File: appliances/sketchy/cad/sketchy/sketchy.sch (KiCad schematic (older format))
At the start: 6 parts, among them J1 Barrel_Jack, M1 Stepper_Motor_bipolar, M2 Stepper_Motor_bipolar, U1 ESP32PICO-KIT

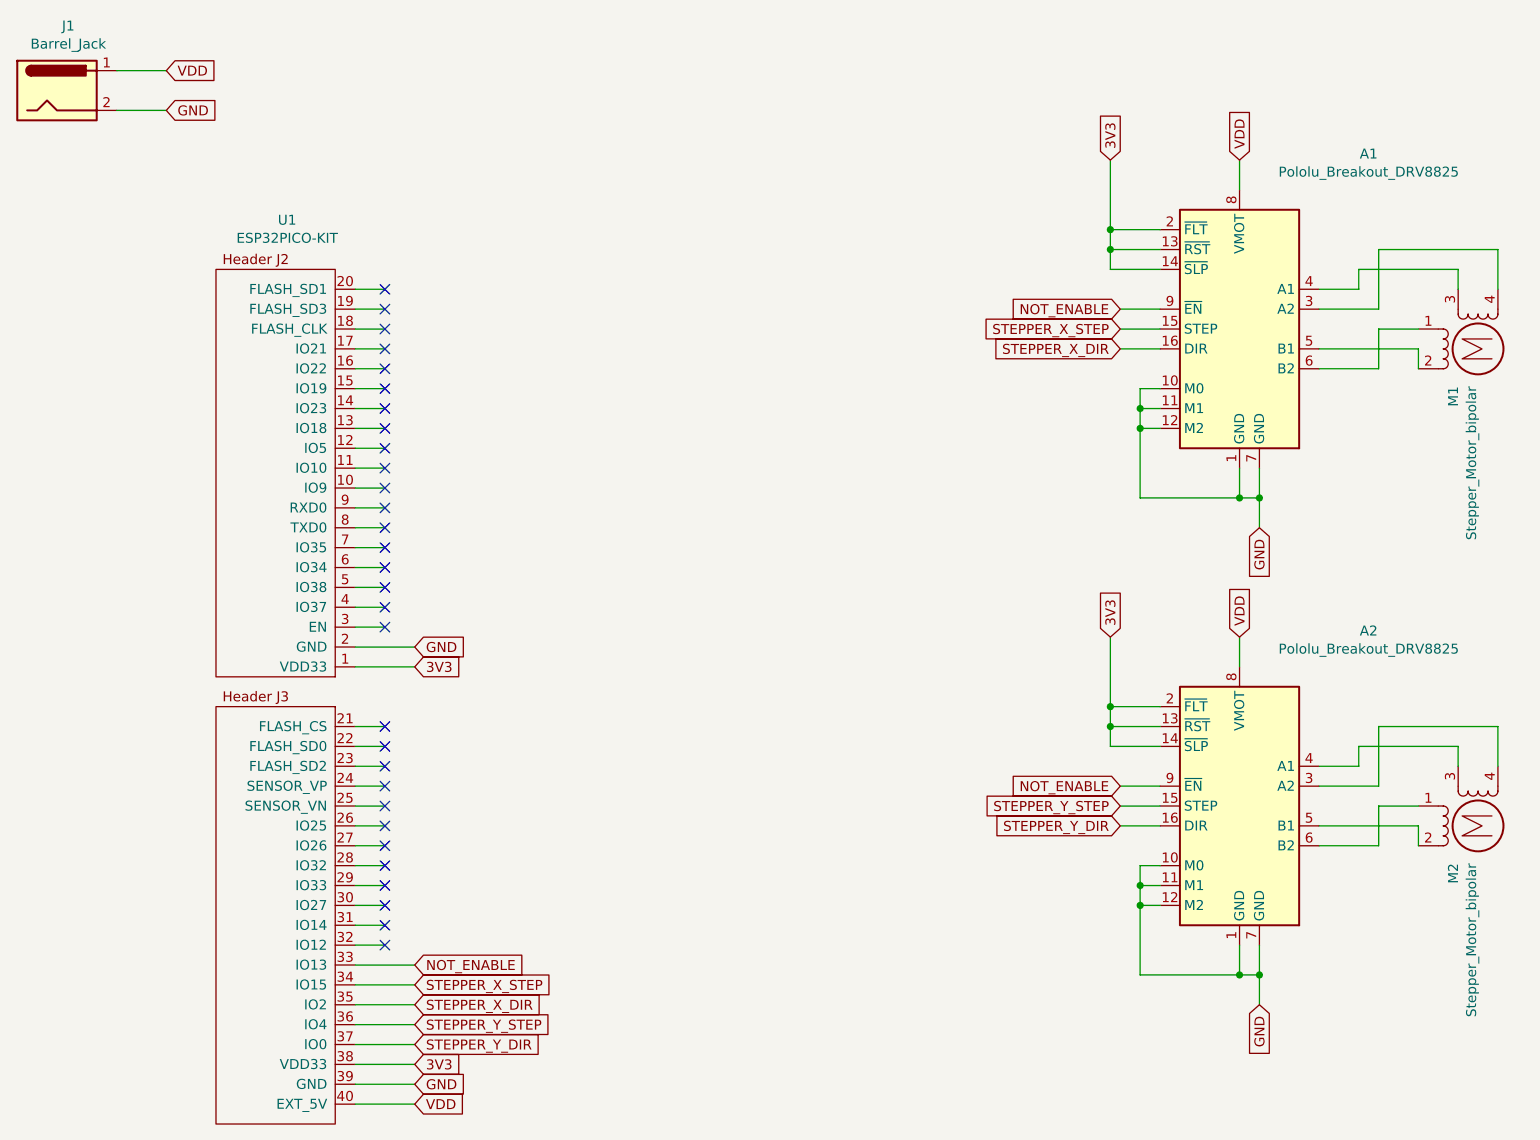
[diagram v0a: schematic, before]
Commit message: Changed stepper driver to the 4988 that I'm actually using, routed all tracks, and added silkscreen text and mounting holes.
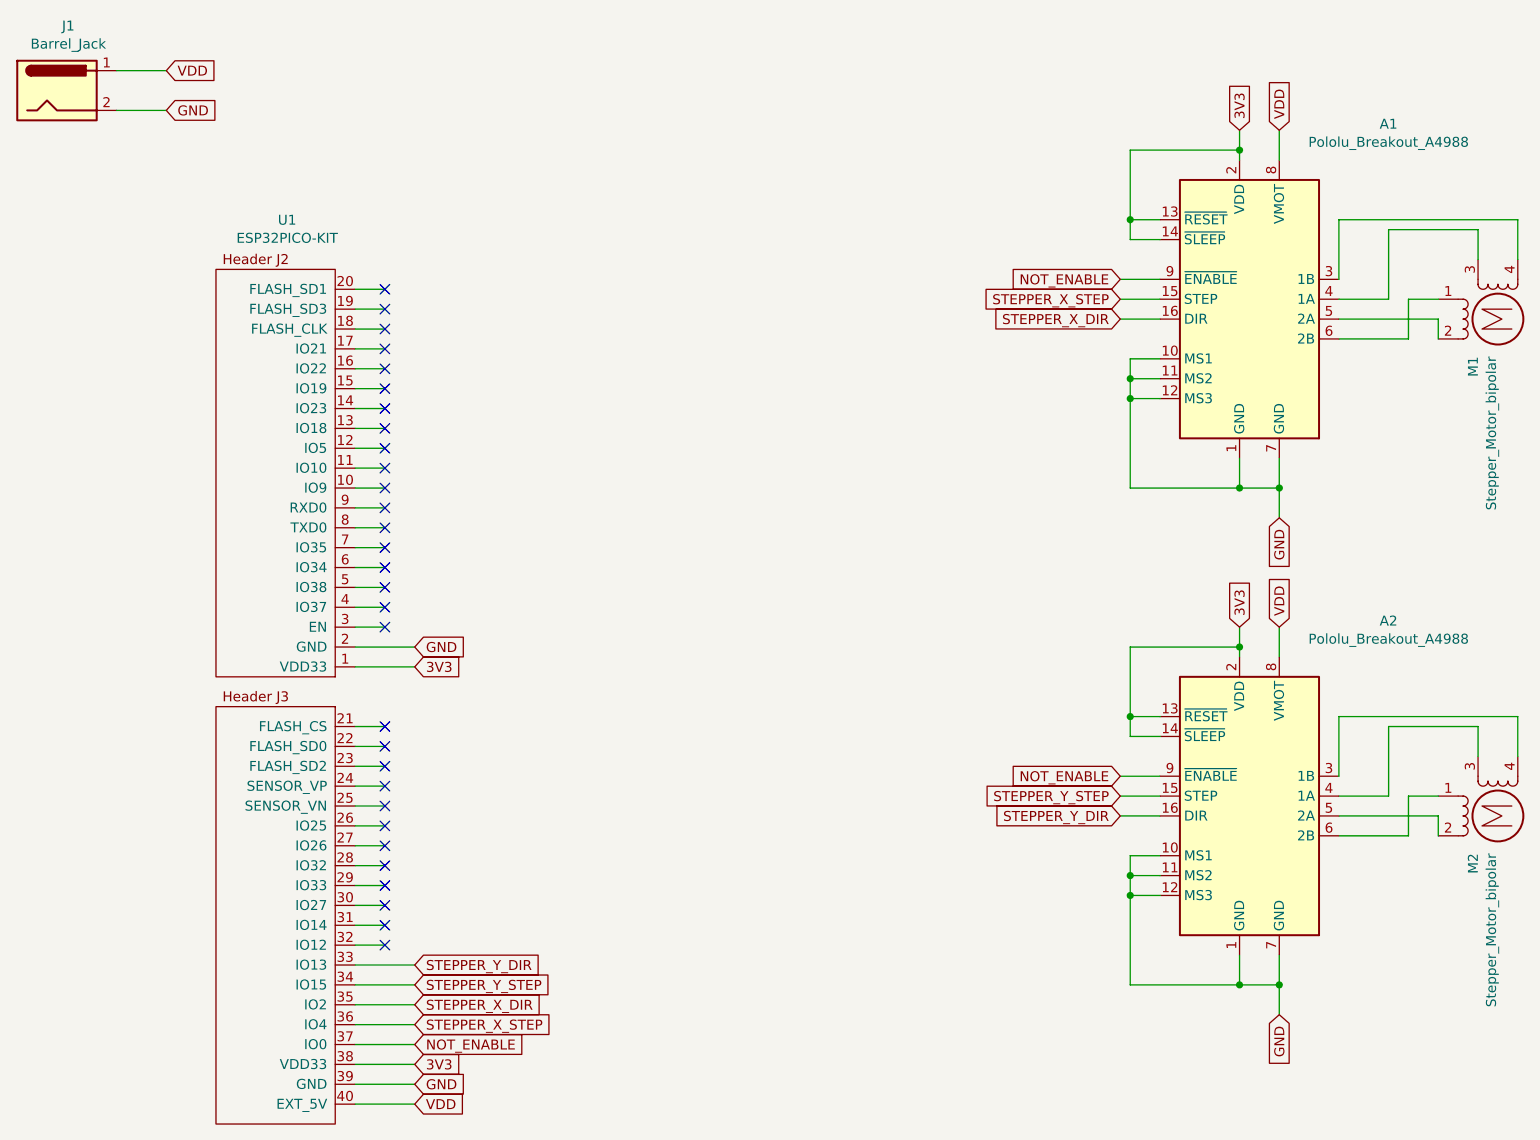
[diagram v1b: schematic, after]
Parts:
- removed A1, A2: Pololu_Breakout_DRV8825, Modules:Pololu_Breakout-16_15.2x20.3mm, symbol Driver_Motor:Pololu_Breakout_DRV8825
- added A1, A2: Pololu_Breakout_A4988, Modules:Pololu_Breakout-16_15.2x20.3mm, symbol Driver_Motor:Pololu_Breakout_A4988
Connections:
- net 3V3: now also A1.13 (~RESET), A1.14 (~SLEEP), A1.2 (VDD), A2.13 (~RESET), A2.14 (~SLEEP), A2.2 (VDD)
- net GND: now also A1.1 (GND), A1.10 (MS1), A1.11 (MS2), A1.12 (MS3), A1.7 (GND), A2.1 (GND), A2.10 (MS1), A2.11 (MS2), A2.12 (MS3), A2.7 (GND)
- net NOT_ENABLE: now also U1.37 (IO0), A1.9 (~ENABLE), A2.9 (~ENABLE); no longer U1.33 (IO13)
- net STEPPER_X_DIR: now also A1.16 (DIR)
- net STEPPER_X_STEP: now also U1.36 (IO4), A1.15 (STEP); no longer U1.34 (IO15)
- net STEPPER_Y_DIR: now also U1.33 (IO13), A2.16 (DIR); no longer U1.37 (IO0)
- net STEPPER_Y_STEP: now also U1.34 (IO15), A2.15 (STEP); no longer U1.36 (IO4)
- net VDD: now also A1.8 (VMOT), A2.8 (VMOT)
- net at M1.4: now also A1.3 (1B)
- net at M1.3: now also A1.4 (1A)
- net at M1.2 (-): now also A1.5 (2A)
- net at M1.1: now also A1.6 (2B)
- net at M2.4: now also A2.3 (1B)
- net at M2.3: now also A2.4 (1A)
- net at M2.2 (-): now also A2.5 (2A)
- net at M2.1: now also A2.6 (2B)
